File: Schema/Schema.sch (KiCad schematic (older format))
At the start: 6 parts

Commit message: Added schema pdf
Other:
- note added: "Automatic Pet Feeder"
- moved on the sheet: IR_Sensor1, IR_Sensor2, M?, R1, SW?, TTGO
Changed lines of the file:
@@
 L ttgo_esp32_correct:TTGO_ESP32_TDISPLAY_V1.1 TTGO
 U 1 1 5EB3D018
-P 2700 3950
-F 0 "TTGO" H 3050 5387 60  0000 C CNN
-F 1 "TTGO_ESP32_TDISPLAY_V1.1" H 3050 5281 60  0000 C CNN
-F 2 "" H 2700 3950 60  0001 C CNN
-F 3 "" H 2700 3950 60  0001 C CNN
-	1    2700 3950
+P 3350 4550
+F 0 "TTGO" H 3700 5987 60  0000 C CNN
+F 1 "TTGO_ESP32_TDISPLAY_V1.1" H 3700 5881 60  0000 C CNN
+F 2 "" H 3350 4550 60  0001 C CNN
+F 3 "" H 3350 4550 60  0001 C CNN
+	1    3350 4550
 	1    0    0    -1
 $EndComp
-Text GLabel 3600 2800 2    50   Input ~ 0
+Text GLabel 4250 3400 2    50   Input ~ 0
 Vcc
-Text GLabel 2500 3500 0    50   Input ~ 0
+Text GLabel 3150 4100 0    50   Input ~ 0
 BUTTON_PIN
-Text GLabel 2500 3300 0    50   Input ~ 0
+Text GLabel 3150 3900 0    50   Input ~ 0
 IR1_PIN
-Text GLabel 2500 3600 0    50   Input ~ 0
+Text GLabel 3150 4200 0    50   Input ~ 0
 IR2_PIN
-Text GLabel 2500 3400 0    50   Input ~ 0
+Text GLabel 3150 4000 0    50   Input ~ 0
 SERVO_PIN
-Text GLabel 6300 2550 0    50   Input ~ 0
+Text GLabel 6950 3150 0    50   Input ~ 0
 IR2_PIN
-Text GLabel 6300 3950 0    50   Input ~ 0
+Text GLabel 6950 4550 0    50   Input ~ 0
 Vcc
 Wire Wire Line
-	4400 2350 4650 2350
+	5050 2950 5300 2950
 $Comp
 L power:GND #PWR?
 U 1 1 5EB540C1
-P 4400 2350
-F 0 "#PWR?" H 4400 2100 50  0001 C CNN
-F 1 "GND" H 4405 2177 50  0000 C CNN
-F 2 "" H 4400 2350 50  0001 C CNN
-F 3 "" H 4400 2350 50  0001 C CNN
-	1    4400 2350
+P 5050 2950
+F 0 "#PWR?" H 5050 2700 50  0001 C CNN
+F 1 "GND" H 5055 2777 50  0000 C CNN
+F 2 "" H 5050 2950 50  0001 C CNN
+F 3 "" H 5050 2950 50  0001 C CNN
+	1    5050 2950
 	0    1    1    0
 $EndComp
-Text GLabel 4650 2250 0    50   Input ~ 0
+Text GLabel 5300 2850 0    50   Input ~ 0
 Vcc
-Text GLabel 4650 2150 0    50   Input ~ 0
+Text GLabel 5300 2750 0    50   Input ~ 0
 SERVO_PIN
 $Comp
 L power:GND #PWR?
 U 1 1 5EB516A9
-P 6300 2250
-F 0 "#PWR?" H 6300 2000 50  0001 C CNN
-F 1 "GND" H 6305 2077 50  0000 C CNN
-F 2 "" H 6300 2250 50  0001 C CNN
-F 3 "" H 6300 2250 50  0001 C CNN
-	1    6300 2250
+P 6950 2850
+F 0 "#PWR?" H 6950 2600 50  0001 C CNN
+F 1 "GND" H 6955 2677 50  0000 C CNN
+F 2 "" H 6950 2850 50  0001 C CNN
+F 3 "" H 6950 2850 50  0001 C CNN
+	1    6950 2850
 	0    1    1    0
 $EndComp
-Text GLabel 6300 2400 0    50   Input ~ 0
+Text GLabel 6950 3000 0    50   Input ~ 0
 Vcc
 $Comp
 L power:GND #PWR?
 U 1 1 5EB50F09
-P 6300 3500
-F 0 "#PWR?" H 6300 3250 50  0001 C CNN
-F 1 "GND" H 6305 3327 50  0000 C CNN
-F 2 "" H 6300 3500 50  0001 C CNN
-F 3 "" H 6300 3500 50  0001 C CNN
-	1    6300 3500
+P 6950 4100
+F 0 "#PWR?" H 6950 3850 50  0001 C CNN
+F 1 "GND" H 6955 3927 50  0000 C CNN
+F 2 "" H 6950 4100 50  0001 C CNN
+F 3 "" H 6950 4100 50  0001 C CNN
+	1    6950 4100
 	0    1    1    0
 $EndComp
-Text GLabel 6300 3650 0    50   Input ~ 0
+Text GLabel 6950 4250 0    50   Input ~ 0
 Vcc
-Text GLabel 6300 3800 0    50   Input ~ 0
+Text GLabel 6950 4400 0    50   Input ~ 0
 IR1_PIN
-Text GLabel 5000 3100 2    50   Input ~ 0
+Text GLabel 5650 3700 2    50   Input ~ 0
 BUTTON_PIN
-Text GLabel 4600 3300 0    50   Input ~ 0
+Text GLabel 5250 3900 0    50   Input ~ 0
 Vcc
 $Comp
 L Switch:SW_Push_Dual SW?
 U 1 1 5EB402BB
-P 4800 3100
-F 0 "SW?" H 4800 3385 50  0000 C CNN
-F 1 "SW_Push_Dual" H 4800 3294 50  0000 C CNN
-F 2 "" H 4800 3300 50  0001 C CNN
-F 3 "~" H 4800 3300 50  0001 C CNN
-	1    4800 3100
+P 5450 3700
+F 0 "SW?" H 5450 3985 50  0000 C CNN
+F 1 "SW_Push_Dual" H 5450 3894 50  0000 C CNN
+F 2 "" H 5450 3900 50  0001 C CNN
+F 3 "~" H 5450 3900 50  0001 C CNN
+	1    5450 3700
 	1    0    0    -1
 $EndComp
@@
 L HW-511:HW-511 IR_Sensor2
 U 1 1 5EB3E7F7
-P 6700 2000
-F 0 "IR_Sensor2" H 6978 1721 50  0000 L CNN
-F 1 "HW-511" H 6978 1630 50  0000 L CNN
-F 2 "" H 6700 2000 50  0001 C CNN
-F 3 "" H 6700 2000 50  0001 C CNN
-	1    6700 2000
+P 7350 2600
+F 0 "IR_Sensor2" H 7628 2321 50  0000 L CNN
+F 1 "HW-511" H 7628 2230 50  0000 L CNN
+F 2 "" H 7350 2600 50  0001 C CNN
+F 3 "" H 7350 2600 50  0001 C CNN
+	1    7350 2600
 	1    0    0    -1
 $EndComp
@@
 L KY-032:KY-032 IR_Sensor1
 U 1 1 5EB45445
-P 6650 3300
-F 0 "IR_Sensor1" H 7128 3021 50  0000 L CNN
-F 1 "KY-032" H 7128 2930 50  0000 L CNN
-F 2 "" H 6800 3350 50  0001 C CNN
-F 3 "" H 6800 3350 50  0001 C CNN
-	1    6650 3300
+P 7300 3900
+F 0 "IR_Sensor1" H 7778 3621 50  0000 L CNN
+F 1 "KY-032" H 7778 3530 50  0000 L CNN
+F 2 "" H 7450 3950 50  0001 C CNN
+F 3 "" H 7450 3950 50  0001 C CNN
+	1    7300 3900
 	1    0    0    -1
 $EndComp
@@
 L Motor:Motor_Servo M?
 U 1 1 5EB482A1
-P 4950 2250
-F 0 "M?" H 5282 2315 50  0000 L CNN
-F 1 "MicroServo" H 5282 2224 50  0000 L CNN
-F 2 "" H 4950 2060 50  0001 C CNN
-F 3 "http://forums.parallax.com/uploads/attachments/46831/74481.png" H 4950 2060 50  0001 C CNN
-	1    4950 2250
+P 5600 2850
+F 0 "M?" H 5932 2915 50  0000 L CNN
+F 1 "MicroServo" H 5932 2824 50  0000 L CNN
+F 2 "" H 5600 2660 50  0001 C CNN
+F 3 "http://forums.parallax.com/uploads/attachments/46831/74481.png" H 5600 2660 50  0001 C CNN
+	1    5600 2850
 	1    0    0    -1
 $EndComp
 Wire Wire Line
-	5000 3600 5000 3300
+	5650 4200 5650 3900
 Wire Wire Line
-	5000 3900 5000 4150
+	5650 4500 5650 4750
 $Comp
 L power:GND #PWR?
 U 1 1 5EA06C5D
-P 5000 4150
-F 0 "#PWR?" H 5000 3900 50  0001 C CNN
-F 1 "GND" H 5005 3977 50  0000 C CNN
-F 2 "" H 5000 4150 50  0001 C CNN
-F 3 "" H 5000 4150 50  0001 C CNN
-	1    5000 4150
+P 5650 4750
+F 0 "#PWR?" H 5650 4500 50  0001 C CNN
+F 1 "GND" H 5655 4577 50  0000 C CNN
+F 2 "" H 5650 4750 50  0001 C CNN
+F 3 "" H 5650 4750 50  0001 C CNN
+	1    5650 4750
 	1    0    0    -1
 $EndComp
@@
 L Device:R R1
 U 1 1 5EA0485A
-P 5000 3750
-F 0 "R1" V 4793 3750 50  0000 C CNN
-F 1 "20k" V 4884 3750 50  0000 C CNN
-F 2 "" V 4930 3750 50  0001 C CNN
-F 3 "~" H 5000 3750 50  0001 C CNN
-	1    5000 3750
+P 5650 4350
+F 0 "R1" V 5443 4350 50  0000 C CNN
+F 1 "20k" V 5534 4350 50  0000 C CNN
+F 2 "" V 5580 4350 50  0001 C CNN
+F 3 "~" H 5650 4350 50  0001 C CNN
+	1    5650 4350
 	1    0    0    -1
 $EndComp
+Text Notes 7350 7500 0    50   ~ 0
+Automatic Pet Feeder
 $EndSCHEMATC

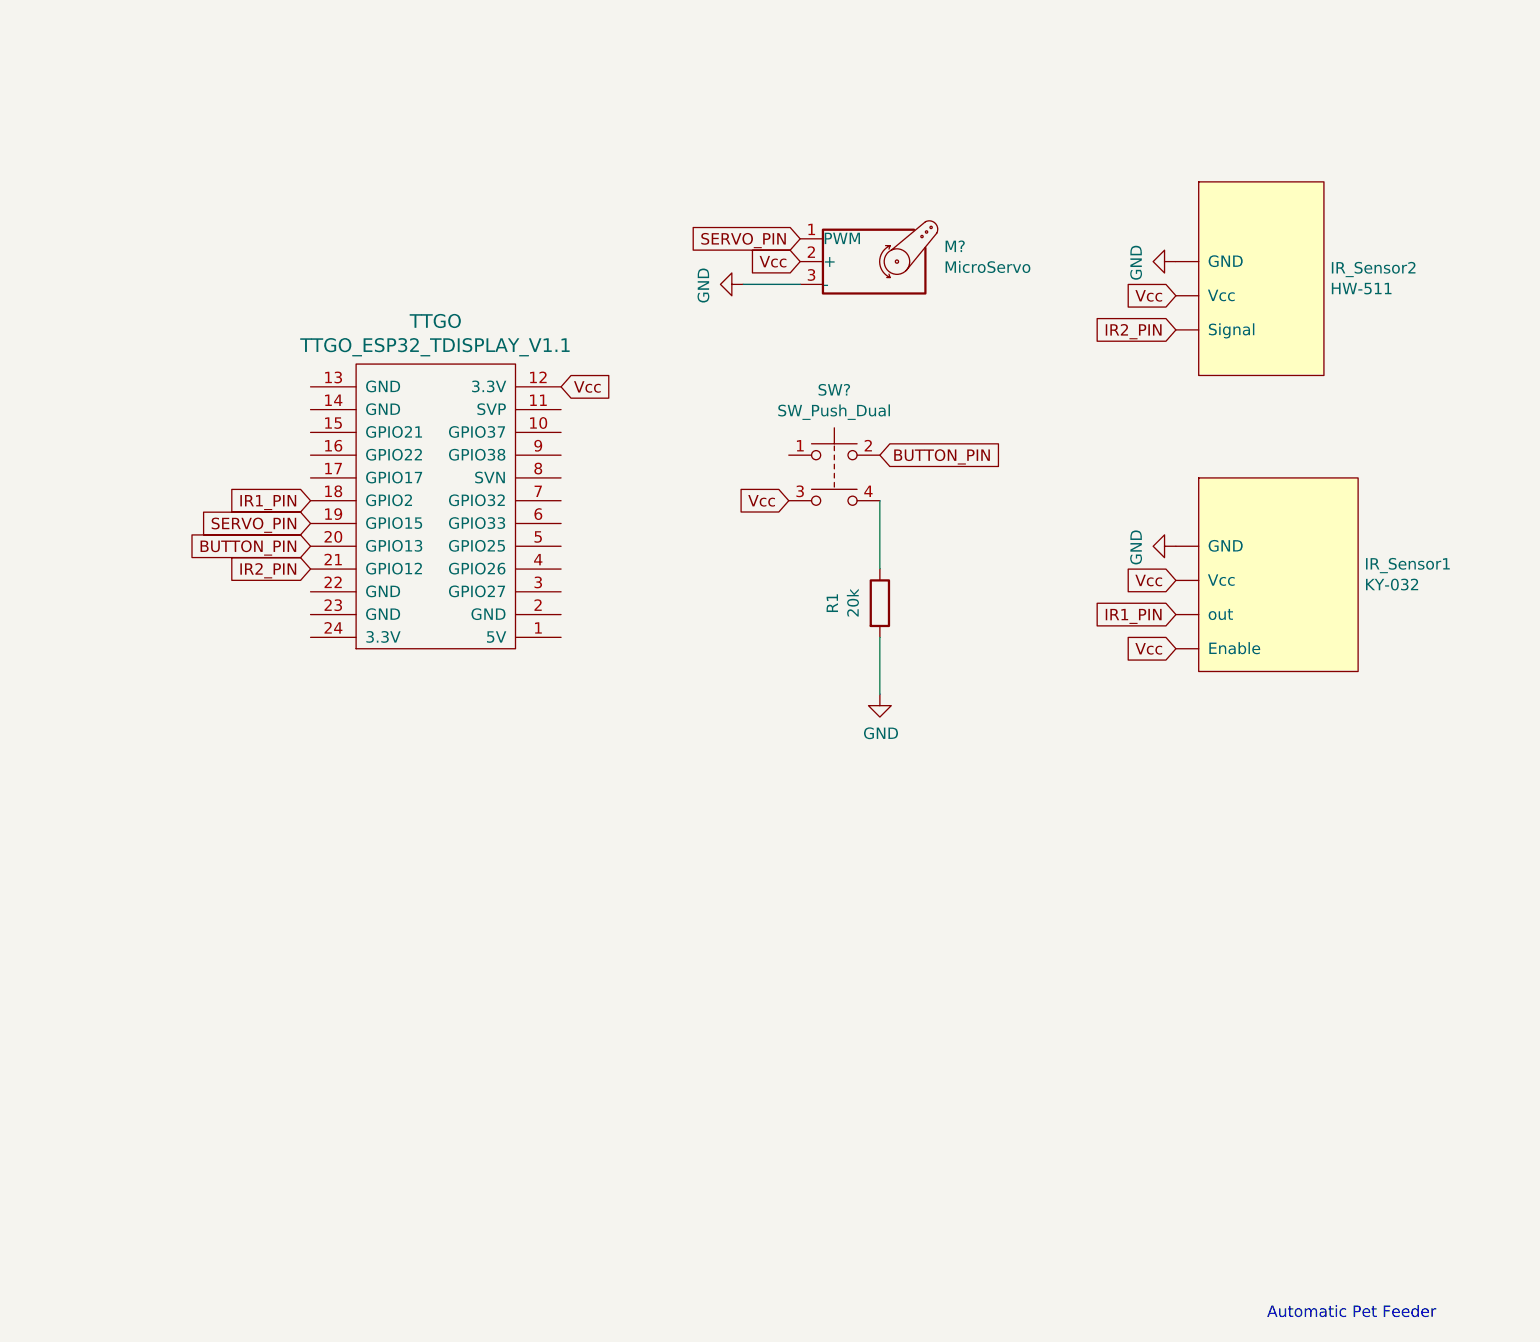
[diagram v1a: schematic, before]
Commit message: Tested Aluminium Foil capsense instead of IR - Kind of works!
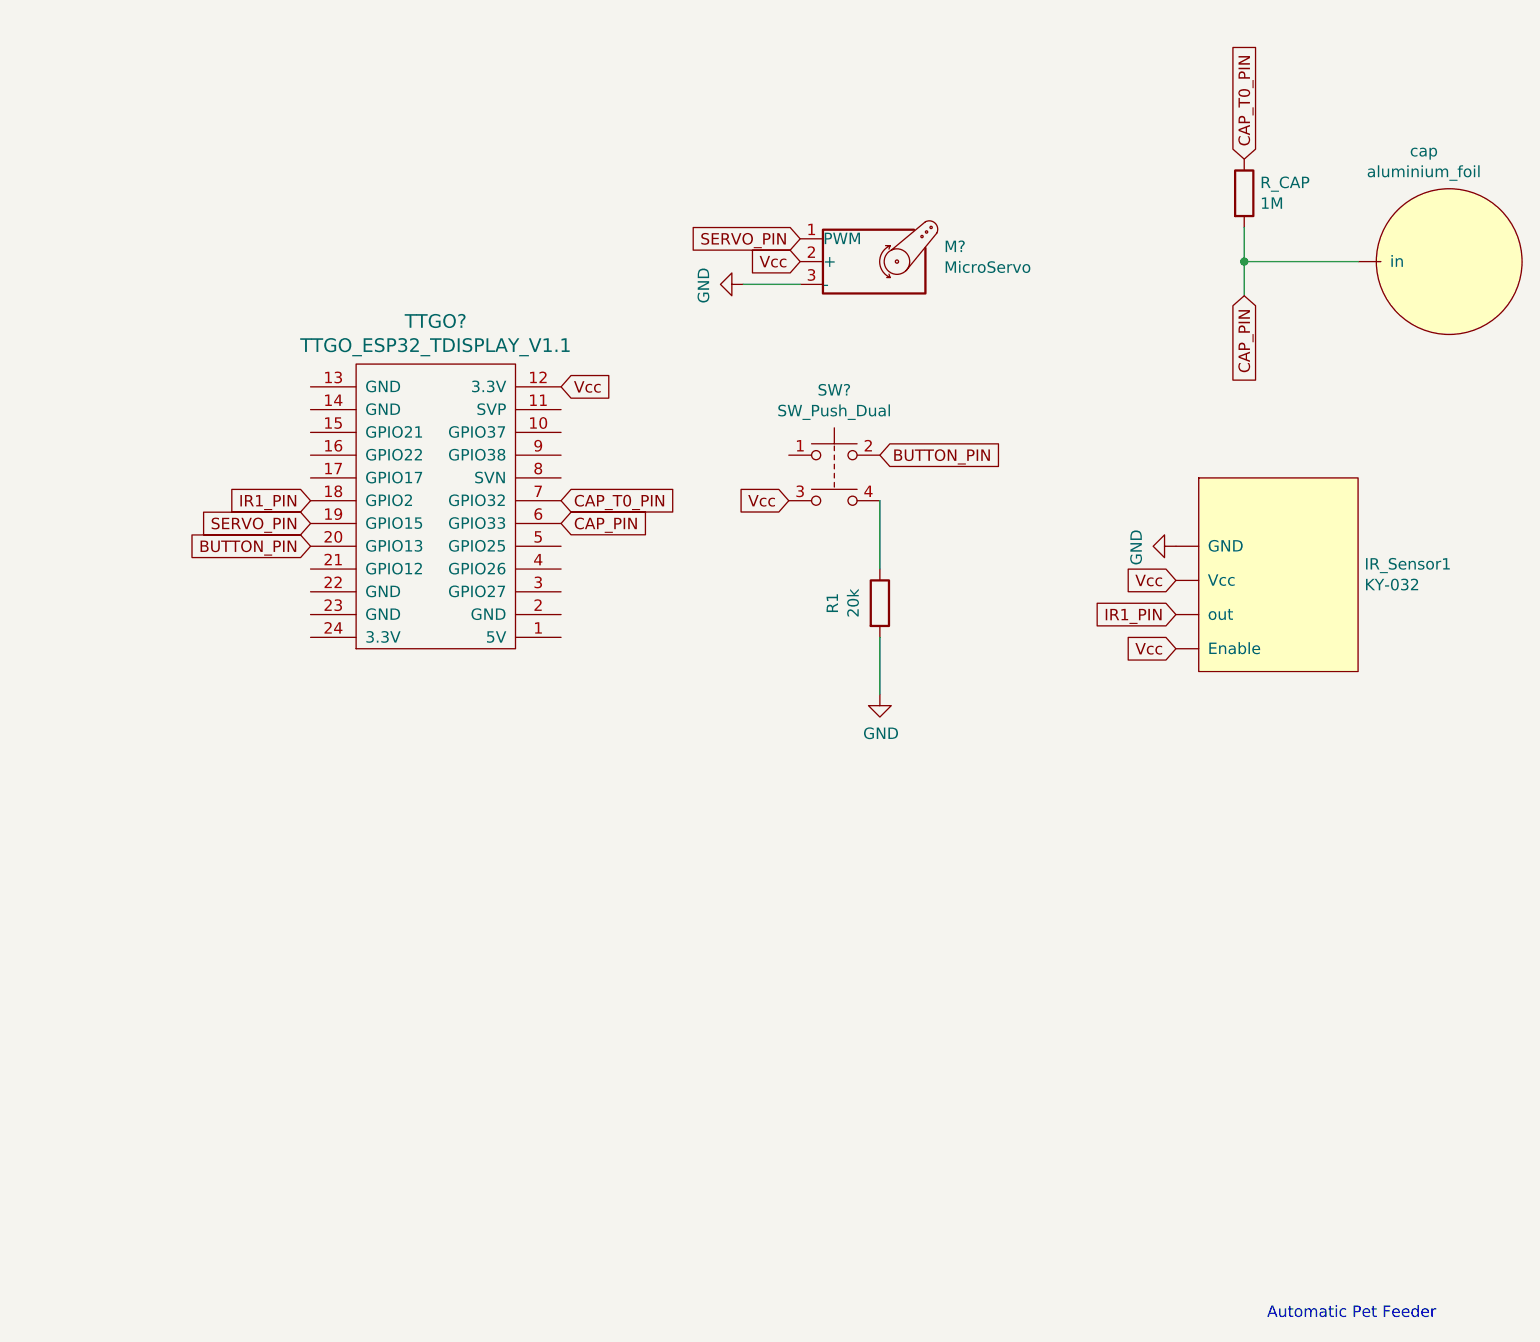
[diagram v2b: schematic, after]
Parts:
- removed IR_Sensor2: HW-511, symbol HW-511:HW-511
- removed TTGO: TTGO_ESP32_TDISPLAY_V1.1, symbol ttgo_esp32_correct:TTGO_ESP32_TDISPLAY_V1.1
- added R_CAP: 1M, symbol Device:R
- added TTGO?: TTGO_ESP32_TDISPLAY_V1.1, symbol ttgo_esp322:TTGO_ESP32_TDISPLAY_V1.1
- added cap: aluminium_foil, symbol capsense:aluminium_foil
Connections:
- net BUTTON_PIN: now also TTGO?.20 (GPIO13)
- net IR1_PIN: now also TTGO?.18 (GPIO2)
- net SERVO_PIN: now also TTGO?.19 (GPIO15)
- net Vcc: now also TTGO?.12 (3.3V)
- new net CAP_PIN: R_CAP.2, TTGO?.6 (GPIO33), cap.~ (in)
- new net CAP_T0_PIN: R_CAP.1, TTGO?.7 (GPIO32)
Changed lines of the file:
@@
 Comment4 ""
 $EndDescr
-$Comp
-L ttgo_esp32_correct:TTGO_ESP32_TDISPLAY_V1.1 TTGO
-U 1 1 5EB3D018
-P 3350 4550
-F 0 "TTGO" H 3700 5987 60  0000 C CNN
-F 1 "TTGO_ESP32_TDISPLAY_V1.1" H 3700 5881 60  0000 C CNN
-F 2 "" H 3350 4550 60  0001 C CNN
-F 3 "" H 3350 4550 60  0001 C CNN
-	1    3350 4550
-	1    0    0    -1
-$EndComp
 Text GLabel 4250 3400 2    50   Input ~ 0
 Vcc
-Text GLabel 3150 4100 0    50   Input ~ 0
-BUTTON_PIN
-Text GLabel 3150 3900 0    50   Input ~ 0
-IR1_PIN
-Text GLabel 3150 4200 0    50   Input ~ 0
-IR2_PIN
-Text GLabel 3150 4000 0    50   Input ~ 0
-SERVO_PIN
-Text GLabel 6950 3150 0    50   Input ~ 0
-IR2_PIN
 Text GLabel 6950 4550 0    50   Input ~ 0
 Vcc
@@
 Text GLabel 5300 2750 0    50   Input ~ 0
 SERVO_PIN
-$Comp
-L power:GND #PWR?
-U 1 1 5EB516A9
-P 6950 2850
-F 0 "#PWR?" H 6950 2600 50  0001 C CNN
-F 1 "GND" H 6955 2677 50  0000 C CNN
-F 2 "" H 6950 2850 50  0001 C CNN
-F 3 "" H 6950 2850 50  0001 C CNN
-	1    6950 2850
-	0    1    1    0
-$EndComp
-Text GLabel 6950 3000 0    50   Input ~ 0
-Vcc
 $Comp
 L power:GND #PWR?
@@
 F 3 "~" H 5450 3900 50  0001 C CNN
 	1    5450 3700
-	1    0    0    -1
-$EndComp
-$Comp
-L HW-511:HW-511 IR_Sensor2
-U 1 1 5EB3E7F7
-P 7350 2600
-F 0 "IR_Sensor2" H 7628 2321 50  0000 L CNN
-F 1 "HW-511" H 7628 2230 50  0000 L CNN
-F 2 "" H 7350 2600 50  0001 C CNN
-F 3 "" H 7350 2600 50  0001 C CNN
-	1    7350 2600
 	1    0    0    -1
 $EndComp
@@
 Text Notes 7350 7500 0    50   ~ 0
 Automatic Pet Feeder
+Text GLabel 4250 4000 2    50   Input ~ 0
+CAP_PIN
+Text GLabel 4250 3900 2    50   Input ~ 0
+CAP_T0_PIN
+$Comp
+L Device:R R_CAP
+U 1 1 5EBEC65D
+P 7250 2550
+F 0 "R_CAP" H 7320 2596 50  0000 L CNN
+F 1 "1M" H 7320 2505 50  0000 L CNN
+F 2 "" V 7180 2550 50  0001 C CNN
+F 3 "~" H 7250 2550 50  0001 C CNN
+	1    7250 2550
+	1    0    0    -1
+$EndComp
+Text GLabel 7250 2400 1    50   Input ~ 0
+CAP_T0_PIN
+Text GLabel 7250 3000 3    50   Input ~ 0
+CAP_PIN
+$Comp
+L capsense:aluminium_foil cap
+U 1 1 5EBEFB27
+P 8200 2300
+F 0 "cap" H 8039 2235 50  0000 C CNN
+F 1 "aluminium_foil" H 8039 2144 50  0000 C CNN
+F 2 "" H 8200 2250 50  0001 C CNN
+F 3 "" H 8200 2250 50  0001 C CNN
+	1    8200 2300
+	1    0    0    -1
+$EndComp
+Wire Wire Line
+	7250 2700 7250 2850
+Wire Wire Line
+	7750 2850 7250 2850
+Connection ~ 7250 2850
+Wire Wire Line
+	7250 2850 7250 3000
+Text GLabel 3150 4000 0    50   Input ~ 0
+SERVO_PIN
+Text GLabel 3150 3900 0    50   Input ~ 0
+IR1_PIN
+Text GLabel 3150 4100 0    50   Input ~ 0
+BUTTON_PIN
+$Comp
+L ttgo_esp322:TTGO_ESP32_TDISPLAY_V1.1 TTGO?
+U 1 1 5EBF4DCE
+P 3350 4550
+F 0 "TTGO?" H 3700 5987 60  0000 C CNN
+F 1 "TTGO_ESP32_TDISPLAY_V1.1" H 3700 5881 60  0000 C CNN
+F 2 "" H 3350 4550 60  0001 C CNN
+F 3 "" H 3350 4550 60  0001 C CNN
+	1    3350 4550
+	1    0    0    -1
+$EndComp
 $EndSCHEMATC
